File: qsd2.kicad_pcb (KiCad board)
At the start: 2 copper layers, 100 x 75 mm, 73 parts, among them J1 5-1814832-1, J2 5-1814832-1, J3 Conn_02x08_Odd_Even, J4 SJ-3524-SMT, U1 SN74LVC1G14DBV, U10 GALI-39, U2 SN74LVC1G14DBV, U3 SN74CBT3253, U4 SN74AC74PW, U5 AD8226ARZ-R7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

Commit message: Very minor change to silkscreen.  Two capacitors 3300pF to 2200pF.
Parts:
- C12, C14: value 3300pF -> 2200pF
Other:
- board text added: "CLK IN"
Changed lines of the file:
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@@
         (effects (font (size 1 1) (thickness 0.15)))
     )
-    (fp_text value "3300pF" (at 5.175 -1.1) (layer "F.SilkS")
+    (fp_text value "2200pF" (at 5.175 -1.1) (layer "F.SilkS")
         (effects (font (size 1 1) (thickness 0.15)))
     )
@@
         (effects (font (size 1 1) (thickness 0.15)))
     )
-    (fp_text value "3300pF" (at -1.63 -1.975 90) (layer "F.SilkS")
+    (fp_text value "2200pF" (at -1.63 -1.975 90) (layer "F.SilkS")
         (effects (font (size 1 1) (thickness 0.15)))
     )
@@
     (effects (font (size 1 1) (thickness 0.15)) (justify left bottom))
   )
+  (gr_text "CLK IN" (at 130.429 42.7736) (layer "F.SilkS")
+    (effects (font (size 1.5 1.5) (thickness 0.15)) (justify left bottom))
+  )
   (gr_text "T41 EXPERIMENTERS PLATFORM" (at 124.7 91.975) (layer "F.SilkS")
     (effects (font (size 2 2) (thickness 0.25)) (justify left bottom))
@@
   (via (at 141.95 68.15) (size 1) (drill 0.5) (layers "F.Cu" "B.Cu") (net 1))
   (via (at 100.6 55.375) (size 1) (drill 0.5) (layers "F.Cu" "B.Cu") (free) (net 1))
-  (via (at 154.575 79.675) (size 0.8) (drill 0.4) (layers "F.Cu" "B.Cu") (free) (net 1))
+  (via (at 154.575 79.675) (size 1) (drill 0.5) (layers "F.Cu" "B.Cu") (free) (net 1))
   (via (at 117.325 56.675) (size 1) (drill 0.5) (layers "F.Cu" "B.Cu") (free) (net 1))
   (via (at 163.9 82.25) (size 1) (drill 0.5) (layers "F.Cu" "B.Cu") (free) (net 1))
@@
   (via (at 134.3 67.175) (size 1) (drill 0.5) (layers "F.Cu" "B.Cu") (free) (net 1))
   (via (at 168.975 65.35) (size 1) (drill 0.5) (layers "F.Cu" "B.Cu") (free) (net 1))
-  (via (at 134.6 49.8) (size 0.8) (drill 0.4) (layers "F.Cu" "B.Cu") (free) (net 1))
+  (via (at 134.6 49.8) (size 1) (drill 0.5) (layers "F.Cu" "B.Cu") (free) (net 1))
   (via (at 163.575 65.85) (size 1) (drill 0.5) (layers "F.Cu" "B.Cu") (free) (net 1))
   (via (at 171.95 51.1) (size 1) (drill 0.5) (layers "F.Cu" "B.Cu") (free) (net 1))

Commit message: Added README.md.
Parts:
- U3: footprint Package_SO:SSOP-16_4.4x5.2mm_P0.65mm -> 16TSOP:DBQ16-L
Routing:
- net GND: track 16.3 -> 19.5 mm
- net Net-(U3-1B2): track 18.4 -> 17.8 mm

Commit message: Updated to version 1.1 PCB.  Very minor changes.
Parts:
- added R16: 0, Resistor_SMD:R_1206_3216Metric, B.Cu at (169.3, 72.6)
- R3: value 220 -> 270
- U3: footprint 16TSOP:DBQ16-L -> Package_SO:TSSOP-16_4.4x5mm_P0.65mm
- U4: footprint SN74AC74PW:SOP65P640X120-14N -> Package_SO:TSSOP-14_4.4x5mm_P0.65mm
- moved U8 2.67 mm to (174.1, 65.9)
- moved U7 2.66 mm to (171.3, 82.7)
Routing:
- net /REF_I: track 4.83 -> 15.8 mm, vias 0 -> 1
- net /REF_Q: track 5.23 -> 14.6 mm, vias 0 -> 1
- net /5V_FILT: track 97.5 -> 102.8 mm
- net GND: vias 88 -> 91
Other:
- board text added: "V1.1"
- board text removed: "V1.0"

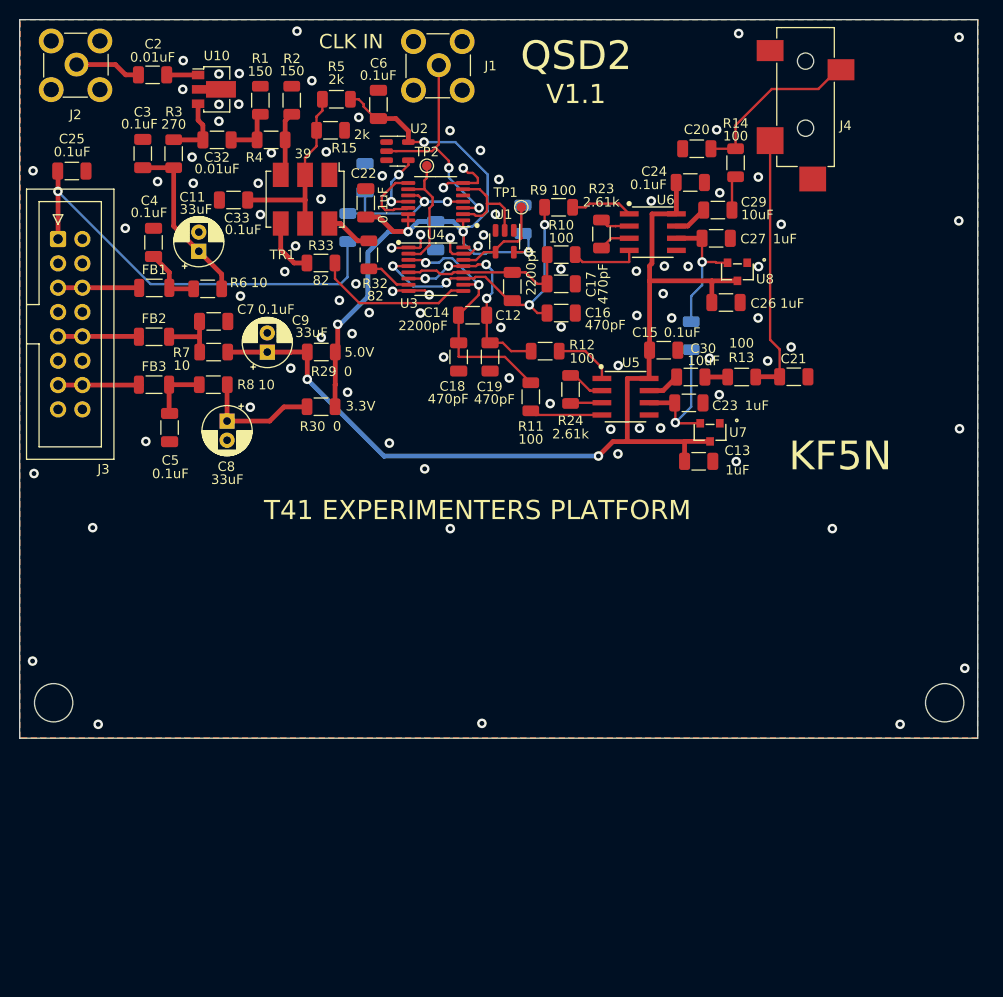
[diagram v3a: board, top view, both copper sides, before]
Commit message: Mostly done rotating flip-flop and detector.
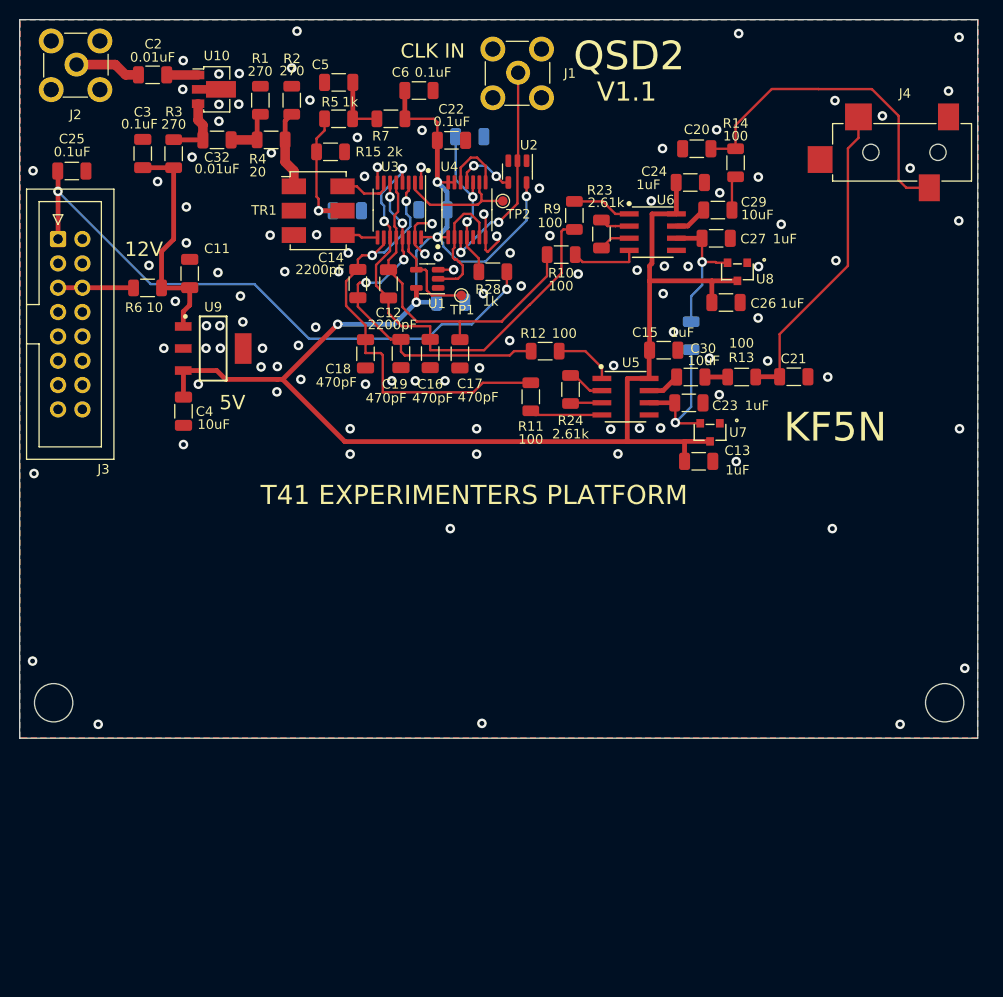
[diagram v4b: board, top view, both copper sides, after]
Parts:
- removed C7: 0.1uF, Capacitor_SMD:C_1206_3216Metric
- removed C8, C9: 33uF, Capacitor_THT:CP_Radial_D5.0mm_P2.00mm
- removed FB1, FB2, FB3: FerrBead, Inductor_SMD:L_1206_3216Metric
- removed R29, R30: 0, Resistor_SMD:R_1206_3216Metric
- removed R32, R33: 82, Resistor_SMD:R_1206_3216Metric
- removed R8: 10, Resistor_SMD:R_1206_3216Metric
- added U9: UA78M05IDCYR, 16TSOP:DCY0004A_N, F.Cu at (119.4, 73.9)
- C11: value 33uF -> 10uF; footprint Capacitor_THT:CP_Radial_D5.0mm_P2.00mm -> Capacitor_SMD:C_1206_3216Metric
- C15, C24: value 0.1uF -> 1uF
- C33: moved to B.Cu
- C4: value 0.1uF -> 10uF
- R1, R2: value 150 -> 270
- R28: moved to F.Cu
- R4: value 39 -> 20
- R5: value 2k -> 1k
- R7: value 10 -> 1k
- moved C5 40.1 mm to (132.5, 46.1), turned to 0 degrees
- moved R7 30.6 mm to (137.9, 50.0)
- moved C4 17.9 mm to (116.3, 80.5)
- moved J4 16.8 mm to (195.1, 53.5), turned to 180 degrees
- moved R28 15.8 mm to (148.6, 65.9), turned to 180 degrees
- moved C16 14.3 mm to (142.1, 74.5), turned to -90 degrees
- moved C12 12.9 mm to (137.7, 67.2)
- moved C17 12.8 mm to (145.2, 74.5), turned to -90 degrees
- moved U2 12.7 mm to (151.2, 55.5), turned to -90 degrees
- moved C14 12.4 mm to (134.5, 67.2), turned to 90 degrees
- moved C33 11.9 mm to (133.4, 59.5), turned to 180 degrees
- moved C31 11.7 mm to (146.2, 51.8), turned to 180 degrees
- moved C1 11.5 mm to (144.2, 69.1), turned to 180 degrees
- moved TP1 11.1 mm to (145.3, 68.4), turned to -90 degrees
- moved C22 11.1 mm to (144.3, 52.2), turned to 180 degrees
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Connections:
- C1 pad 2: /QSD_V -> /5V_FILT
- C10 pad 2: /QSD_V -> /5V_FILT
- C22 pad 2: /QSD_V -> /5V_FILT
- C33 pad 2: Net-(TR1-NOCONN) -> Net-(C33-Pad2)
- C4 pad 1: GND -> /5V_FILT
- C4 pad 2: Net-(C4-Pad2) -> GND
- C5 pad 1: Net-(C5-Pad1) -> GND
- C5 pad 2: GND -> Net-(C5-Pad2)
- C6 pad 2: /QSD_V -> /5V_FILT
- J3 pad 10: /5_0V -> unconnected-(J3-Pin_10-Pad10)
- J3 pad 13: /3_3V -> unconnected-(J3-Pin_13-Pad13)
- J3 pad 14: /3_3V -> unconnected-(J3-Pin_14-Pad14)
- J3 pad 9: /5_0V -> unconnected-(J3-Pin_9-Pad9)
- R15 pad 2: Net-(TR1-NOCONN) -> Net-(C33-Pad2)
- R5 pad 1: Net-(TR1-NOCONN) -> Net-(C33-Pad2)
- R5 pad 2: /QSD_V -> Net-(C5-Pad2)
- R6 pad 1: Net-(C4-Pad2) -> /12_0V
- R7 pad 1: Net-(C7-Pad1) -> Net-(C5-Pad2)
- TR1 pad 1: GND -> Net-(R2-Pad1)
- TR1 pad 2: Net-(TR1-NOCONN) -> unconnected-(TR1-NOCONN-Pad2)
- TR1 pad 3: Net-(R2-Pad1) -> GND
- TR1 pad 4: Net-(R33-Pad1) -> Net-(U3-2A)
- TR1 pad 5: Net-(TR1-NOCONN) -> Net-(C33-Pad2)
- TR1 pad 6: Net-(R32-Pad1) -> Net-(U3-1A)
- U1 pad 5: /QSD_V -> /5V_FILT
- U2 pad 5: /QSD_V -> /5V_FILT
- U3 pad 16: /QSD_V -> /5V_FILT
- U4 pad 1: /QSD_V -> /5V_FILT
- U4 pad 13: /QSD_V -> /5V_FILT
- U4 pad 14: /QSD_V -> /5V_FILT
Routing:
- net /QSD_V: track 77.3 -> 0.00 mm, vias 5 -> 0
- net /5V_FILT: track 102.8 -> 175.9 mm, vias 2 -> 5
- net Net-(TR1-NOCONN): track 19.7 -> 0.00 mm
- net Net-(U3-1B4): track 27.7 -> 46.9 mm
- net /SET: track 45.4 -> 64.3 mm, vias 1 -> 2
- net Net-(U3-1B2): track 17.8 -> 36.1 mm
- net Net-(U3-1B3): track 31.4 -> 49.2 mm, vias 4 -> 2
- net Net-(C20-Pad2): track 18.4 -> 35.0 mm
- net Net-(U3-1B1): track 21.8 -> 38.0 mm
- net Net-(C33-Pad2): track 0.00 -> 14.1 mm, vias 0 -> 1
- net /3_3V_FILT: track 12.8 -> 0.00 mm
- net Net-(U3-2A): track 16.4 -> 3.77 mm
- net /5_0V: track 8.46 -> 0.00 mm
- net /3_3V: track 8.46 -> 0.00 mm
- net Net-(C4-Pad2): track 6.54 -> 0.00 mm
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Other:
- board text added: "12V"
- board text added: "5V"
- board text removed: "3.3V"
- board text removed: "5.0V"

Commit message: Gerbers done, ready to release V1.1.
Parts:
- added C7: 10uF, Capacitor_SMD:C_1206_3216Metric, F.Cu at (115.5, 64.7)
- C11: value 10uF -> 0.1uF
- R16: value 0 -> DNP
- moved C11 8.15 mm to (111.1, 71.8), turned to -90 degrees
- moved J2 0.85 mm to (105.0, 45.2)
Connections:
- C11 pad 1: /12V_FILT -> /12_0V
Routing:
- net /12_0V: track 7.89 -> 10.6 mm
- net /12V_FILT: track 23.6 -> 22.1 mm
- net GND: vias 107 -> 108
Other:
- board text added: "RF INPUT"

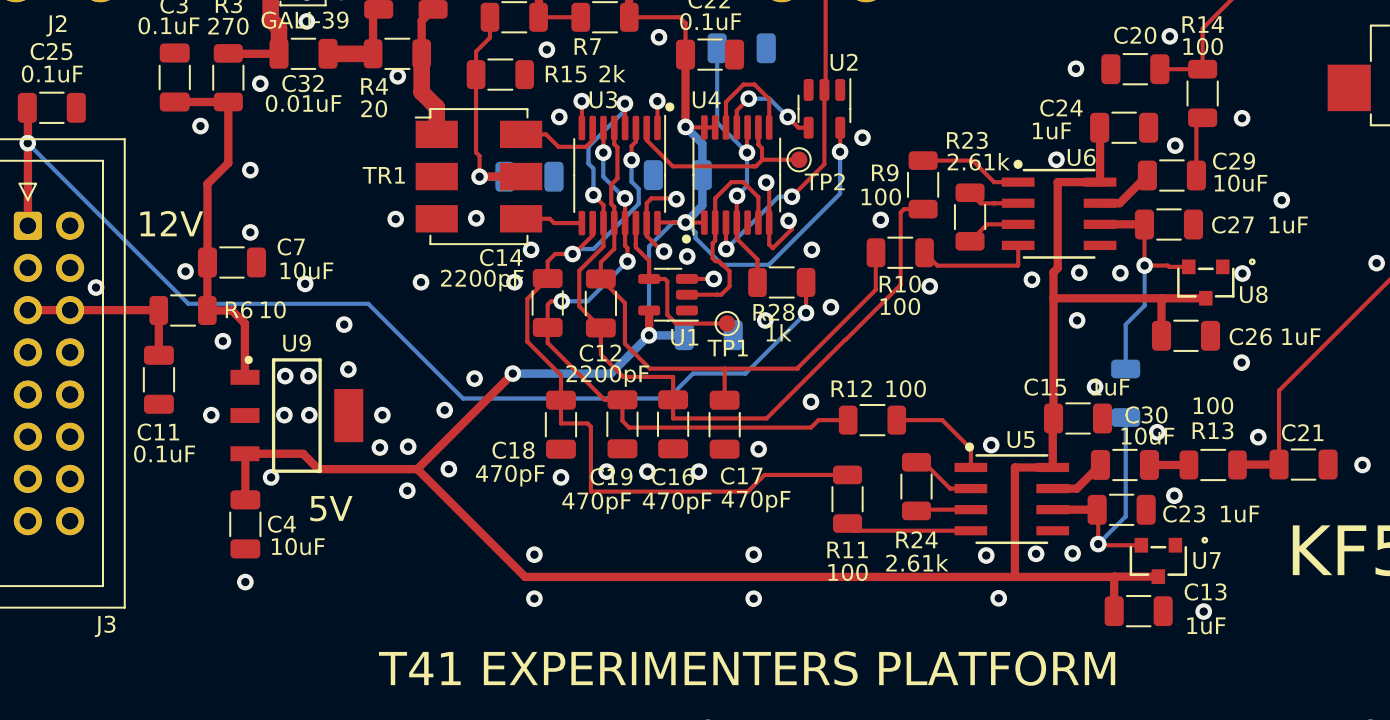
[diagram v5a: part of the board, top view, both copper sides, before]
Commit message: Minor clean-up of a few vias.
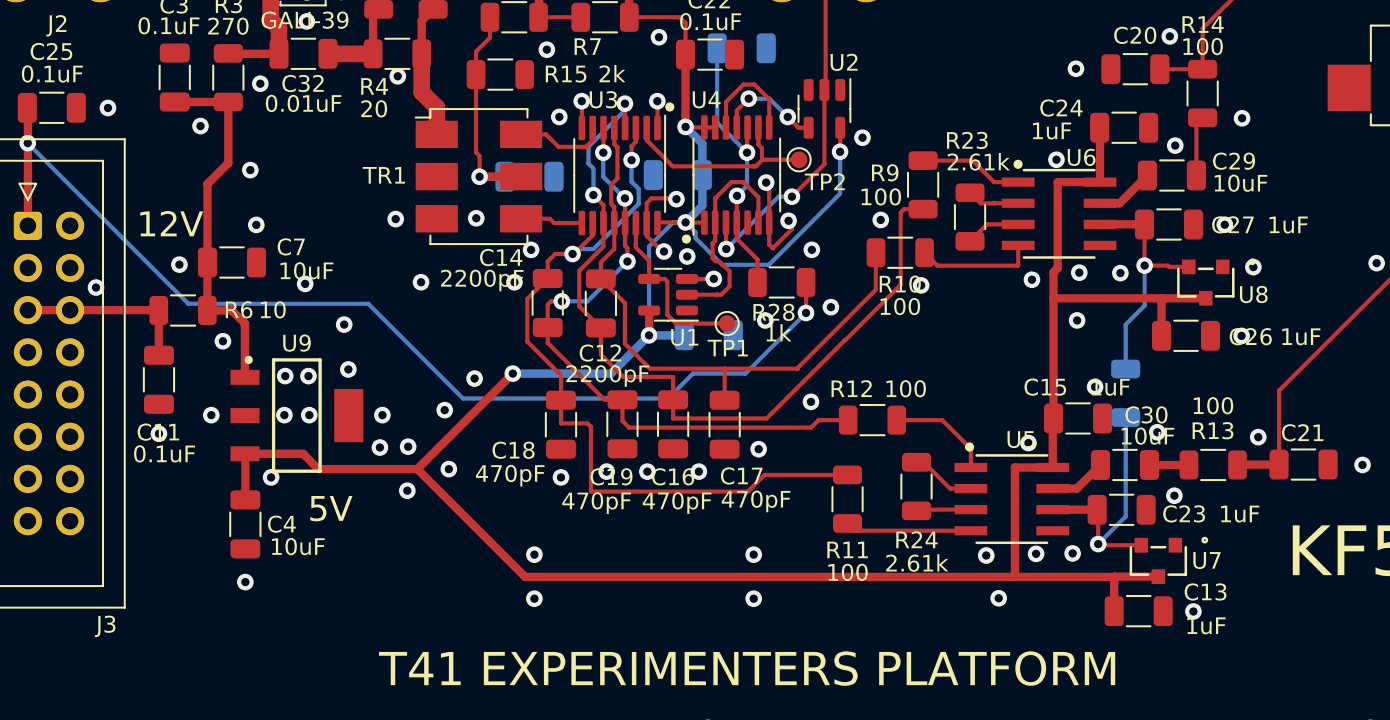
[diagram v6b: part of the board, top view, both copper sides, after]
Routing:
- net GND: vias 108 -> 110
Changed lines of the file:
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@@
   (via (at 184.025 92.725) (size 1) (drill 0.5) (layers "F.Cu" "B.Cu") (free) (net 1))
   (via (at 133.7 82.3) (size 1) (drill 0.5) (layers "F.Cu" "B.Cu") (free) (net 1))
-  (via (at 112.7 65.25) (size 1) (drill 0.5) (layers "F.Cu" "B.Cu") (free) (net 1))
+  (via (at 112.33 64.84) (size 1) (drill 0.5) (layers "F.Cu" "B.Cu") (free) (net 1))
   (via (at 197.85 107.3) (size 1) (drill 0.5) (layers "F.Cu" "B.Cu") (free) (net 1))
   (via (at 126.1 75.8) (size 1) (drill 0.5) (layers "F.Cu" "B.Cu") (free) (net 1))
-  (via (at 157.5 66.15) (size 1) (drill 0.5) (layers "F.Cu" "B.Cu") (free) (net 1))
+  (via (at 156.98 66.09) (size 1) (drill 0.5) (layers "F.Cu" "B.Cu") (free) (net 1))
   (via (at 172.275 57.675) (size 1) (drill 0.5) (layers "F.Cu" "B.Cu") (free) (net 1))
   (via (at 150.35 73.1) (size 1) (drill 0.5) (layers "F.Cu" "B.Cu") (free) (net 1))
   (via (at 142.9 64.35) (size 1) (drill 0.5) (layers "F.Cu" "B.Cu") (free) (net 1))
+  (via (at 108.03 55.41) (size 1) (drill 0.5) (layers "F.Cu" "B.Cu") (free) (net 1))
   (via (at 166.1 82.225) (size 1) (drill 0.5) (layers "F.Cu" "B.Cu") (free) (net 1))
-  (via (at 116.6 62.9) (size 1) (drill 0.5) (layers "F.Cu" "B.Cu") (free) (net 1))
+  (via (at 116.96 62.45) (size 1) (drill 0.5) (layers "F.Cu" "B.Cu") (free) (net 1))
   (via (at 166.37 68.199) (size 1) (drill 0.5) (layers "F.Cu" "B.Cu") (free) (net 1))
   (via (at 133.5 63.95) (size 1) (drill 0.5) (layers "F.Cu" "B.Cu") (free) (net 1))
@@
   (via (at 166.3 53.05) (size 1) (drill 0.5) (layers "F.Cu" "B.Cu") (free) (net 1))
   (via (at 161.65 84.925) (size 1) (drill 0.5) (layers "F.Cu" "B.Cu") (free) (net 1))
-  (via (at 178.689 60.96) (size 1) (drill 0.5) (layers "F.Cu" "B.Cu") (free) (net 1))
+  (via (at 175.26 62.44) (size 1) (drill 0.5) (layers "F.Cu" "B.Cu") (free) (net 1))
   (via (at 122.5 71.15) (size 1) (drill 0.5) (layers "F.Cu" "B.Cu") (free) (net 1))
   (via (at 143.6 77.3) (size 1) (drill 0.5) (layers "F.Cu" "B.Cu") (free) (net 1))
@@
   (via (at 120 50.2) (size 1) (drill 0.5) (layers "F.Cu" "B.Cu") (free) (net 1))
   (via (at 191.1 113.15) (size 1) (drill 0.5) (layers "F.Cu" "B.Cu") (free) (net 1))
+  (via (at 111.1 75.02) (size 1) (drill 0.5) (layers "F.Cu" "B.Cu") (free) (net 1))
   (via (at 118.7 71.55) (size 1) (drill 0.5) (layers "F.Cu" "B.Cu") (free) (net 1))
-  (via (at 176.325 65.375) (size 1) (drill 0.5) (layers "F.Cu" "B.Cu") (free) (net 1))
+  (via (at 176.98 64.99) (size 1) (drill 0.5) (layers "F.Cu" "B.Cu") (free) (net 1))
   (via (at 177.275 75.225) (size 1) (drill 0.5) (layers "F.Cu" "B.Cu") (free) (net 1))
   (via (at 132.5 65.9) (size 1) (drill 0.5) (layers "F.Cu" "B.Cu") (free) (net 1))
@@
   (via (at 116.6 59.15) (size 1) (drill 0.5) (layers "F.Cu" "B.Cu") (free) (net 1))
   (via (at 163.9 82.25) (size 1) (drill 0.5) (layers "F.Cu" "B.Cu") (free) (net 1))
-  (via (at 173.99 85.725) (size 1) (drill 0.5) (layers "F.Cu" "B.Cu") (free) (net 1))
+  (via (at 173.37 85.72) (size 1) (drill 0.5) (layers "F.Cu" "B.Cu") (free) (net 1))
   (via (at 116.275 43.875) (size 1) (drill 0.5) (layers "F.Cu" "B.Cu") (free) (net 1))
   (via (at 172.225 78.75) (size 1) (drill 0.5) (layers "F.Cu" "B.Cu") (free) (net 1))
@@
   (via (at 163.65 65.75) (size 1) (drill 0.5) (layers "F.Cu" "B.Cu") (free) (net 1))
   (via (at 197.26 41.44) (size 1) (drill 0.5) (layers "F.Cu" "B.Cu") (free) (net 1))
-  (via (at 161.2 75.7) (size 1) (drill 0.5) (layers "F.Cu" "B.Cu") (free) (net 1))
+  (via (at 163.44 75.58) (size 1) (drill 0.5) (layers "F.Cu" "B.Cu") (free) (net 1))
   (via (at 176.3 56.03) (size 1) (drill 0.5) (layers "F.Cu" "B.Cu") (free) (net 1))
   (via (at 146.9 82.3) (size 1) (drill 0.5) (layers "F.Cu" "B.Cu") (free) (net 1))
@@
   (via (at 166.5 65.325) (size 1) (drill 0.5) (layers "F.Cu" "B.Cu") (free) (net 1))
   (via (at 189.25 49.65) (size 1) (drill 0.5) (layers "F.Cu" "B.Cu") (free) (net 1))
-  (via (at 176.276 70.739) (size 1) (drill 0.5) (layers "F.Cu" "B.Cu") (free) (net 1))
+  (via (at 176.27 69.13) (size 1) (drill 0.5) (layers "F.Cu" "B.Cu") (free) (net 1))
   (via (at 120.1 71.55) (size 1) (drill 0.5) (layers "F.Cu" "B.Cu") (free) (net 1))
   (via (at 197.3 82.3) (size 1) (drill 0.5) (layers "F.Cu" "B.Cu") (free) (net 1))

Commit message: Ready to publish version 1.1.
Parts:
- C20, C21: value Not used -> DNP
- U5, U6: footprint AD8129ARZ:R_8_ADI -> 16TSOP:R_8_ADI
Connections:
- TR1 pad 2: unconnected-(TR1-NOCONN-Pad2) -> Net-(C33-Pad2)
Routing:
- net Net-(C33-Pad2): track 14.1 -> 16.6 mm
- net GND: vias 110 -> 111
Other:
- board text added: "IQ OUTPUT"

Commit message: Initial commit.
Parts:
- U3: footprint Package_SO:TSSOP-16_4.4x5mm_P0.65mm -> Package_SO:SOIC-16_3.9x9.9mm_P1.27mm
- U4: footprint Package_SO:TSSOP-14_4.4x5mm_P0.65mm -> Package_SO:SOIC-14_3.9x8.7mm_P1.27mm
- U5, U6: footprint 16TSOP:R_8_ADI -> AD8226:R_8_ADI
- moved TP2 6.17 mm to (155.8, 58.8)
- moved R9 4.83 mm to (160.5, 56.6), turned to 0 degrees
- moved U2 4.80 mm to (155.3, 53.0)
- moved U4 4.25 mm to (150.1, 59.5)
- moved R10 2.79 mm to (157.7, 66.1)
- moved TR1 1.90 mm to (128.5, 59.5)
- moved C33 1.53 mm to (131.9, 59.5)
- moved C10 1.39 mm to (143.7, 59.5)
- turned R28 to 0 degrees
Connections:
- TR1 pad 2: Net-(C33-Pad2) -> (no net)
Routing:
- net GND: track 16.3 -> 4.17 mm, vias 111 -> 107
- net Net-(C33-Pad2): track 16.6 -> 5.74 mm
- net Net-(U3-1B3): track 49.2 -> 58.6 mm
- net /CLK1: track 23.3 -> 30.4 mm
- net /FB2: track 6.63 -> 0.00 mm, vias 0 -> 2
- net /5V_FILT: track 175.9 -> 182.3 mm
- net /LO_Q: track 12.8 -> 18.4 mm
- net /PREN: track 17.1 -> 21.0 mm
- net /FB1: track 13.6 -> 16.3 mm
- net Net-(U6-IN-): track 6.26 -> 3.63 mm
- net Net-(U3-1B4): track 46.9 -> 48.9 mm, vias 2 -> 3
- net Net-(U6-IN+): track 7.16 -> 5.36 mm
- net Net-(U3-1A): track 5.52 -> 6.85 mm
- net /SET: track 64.3 -> 63.2 mm
- net Net-(U3-1B2): track 36.1 -> 35.5 mm
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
